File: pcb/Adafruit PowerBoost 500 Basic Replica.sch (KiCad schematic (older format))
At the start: 24 parts, among them CN1 USBA, J1 HEADER, J2 PWR OUT CONN, Q1 MMUN2133LT1G, U1 TPS61090RSAR

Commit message: Agregada la propuesta
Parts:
- BT1: footprint (none) -> Connector_JST:JST_EH_S2B-EH_1x02_P2.50mm_Horizontal
- C1, C2, C3: footprint (none) -> Capacitor_SMD:C_0805_2012Metric
- C4: footprint (none) -> Capacitor_SMD:C_1206_3216Metric
- CN1: footprint (none) -> Connector_USB:USB_A_CONNFLY_DS1095-WNR0
- D1, D2: footprint (none) -> LED_SMD:LED_0805_2012Metric
- J1: footprint (none) -> Connector_PinHeader_1.00mm:PinHeader_1x06_P1.00mm_Vertical
- J2: footprint (none) -> Connector_PinHeader_1.00mm:PinHeader_1x02_P1.00mm_Vertical
- L1: footprint (none) -> Inductor_SMD:L_TDK_VLP8040
- Q1: footprint (none) -> Package_TO_SOT_SMD:SOT-23
- R1, R10, R11, R2, R3, R4, R5, R6, R7, R8, R9: footprint (none) -> Resistor_SMD:R_0805_2012Metric
- U1: footprint (none) -> Package_DFN_QFN:QFN-16-1EP_4x4mm_P0.65mm_EP2.1x2.1mm
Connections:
- net +5V: no longer C3.1, C4.1, J2.1 (Pin_1), R4.1, U1.16 (VOUT)
- net GND: no longer U1.12 (LBO)
- net at U1.7 (PGND): now also U1.12 (LBO)
- new net: C3.1, C4.1, J2.1 (Pin_1), R4.1, U1.16 (VOUT)
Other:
- note added: "Etapa de Regulación"
- note added: "Indicador de 5V a la salida\n(encendido)"
- note added: "Indicador de Batería Baja"
- note added: "Salida Cargador USB"
- moved on the sheet: BT1, C1, C2, C3, C4, CN1, D1, D2, J1, J2, L1, Q1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

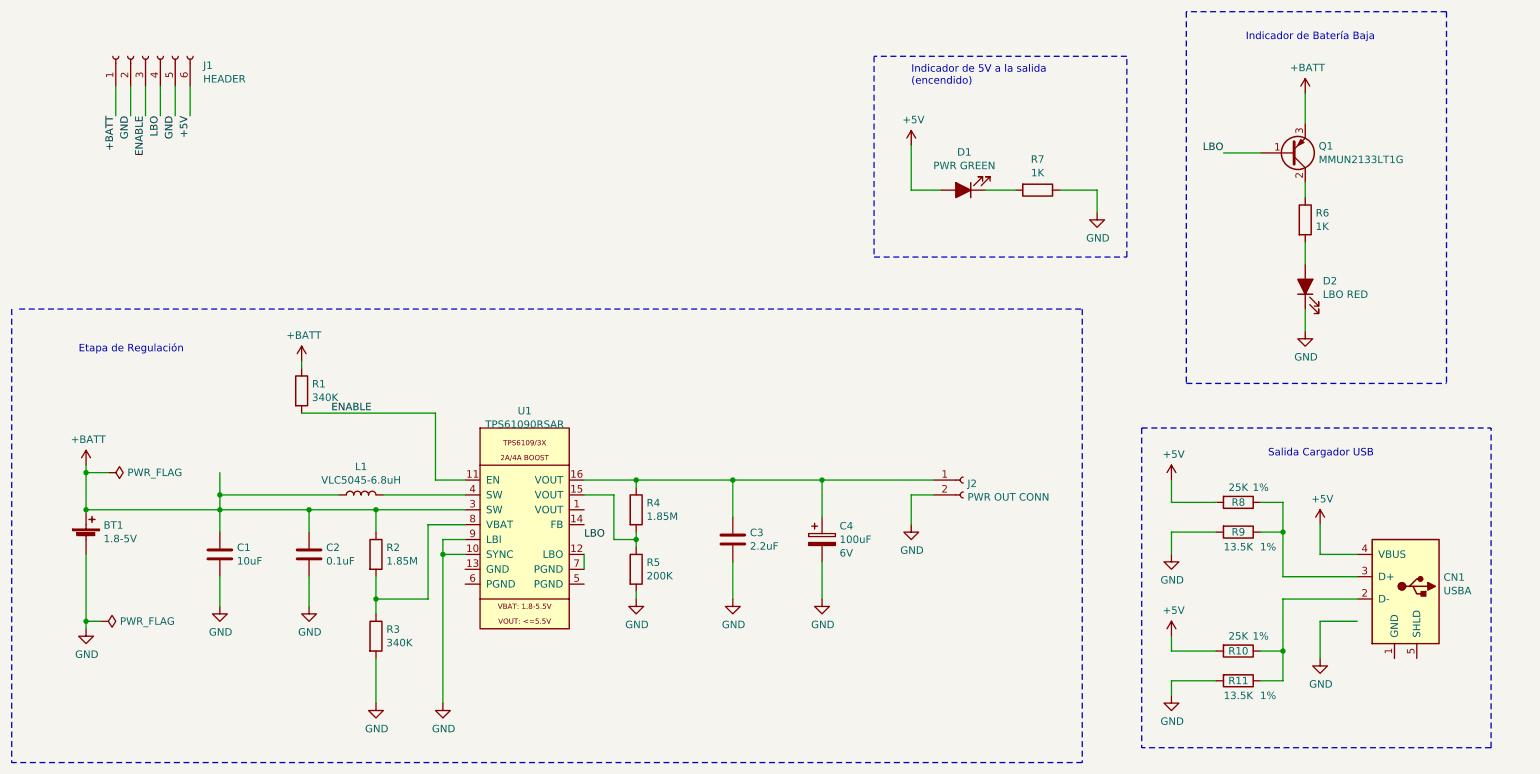
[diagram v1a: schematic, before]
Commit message: Correcciones de acuerdo a checklist esquematico
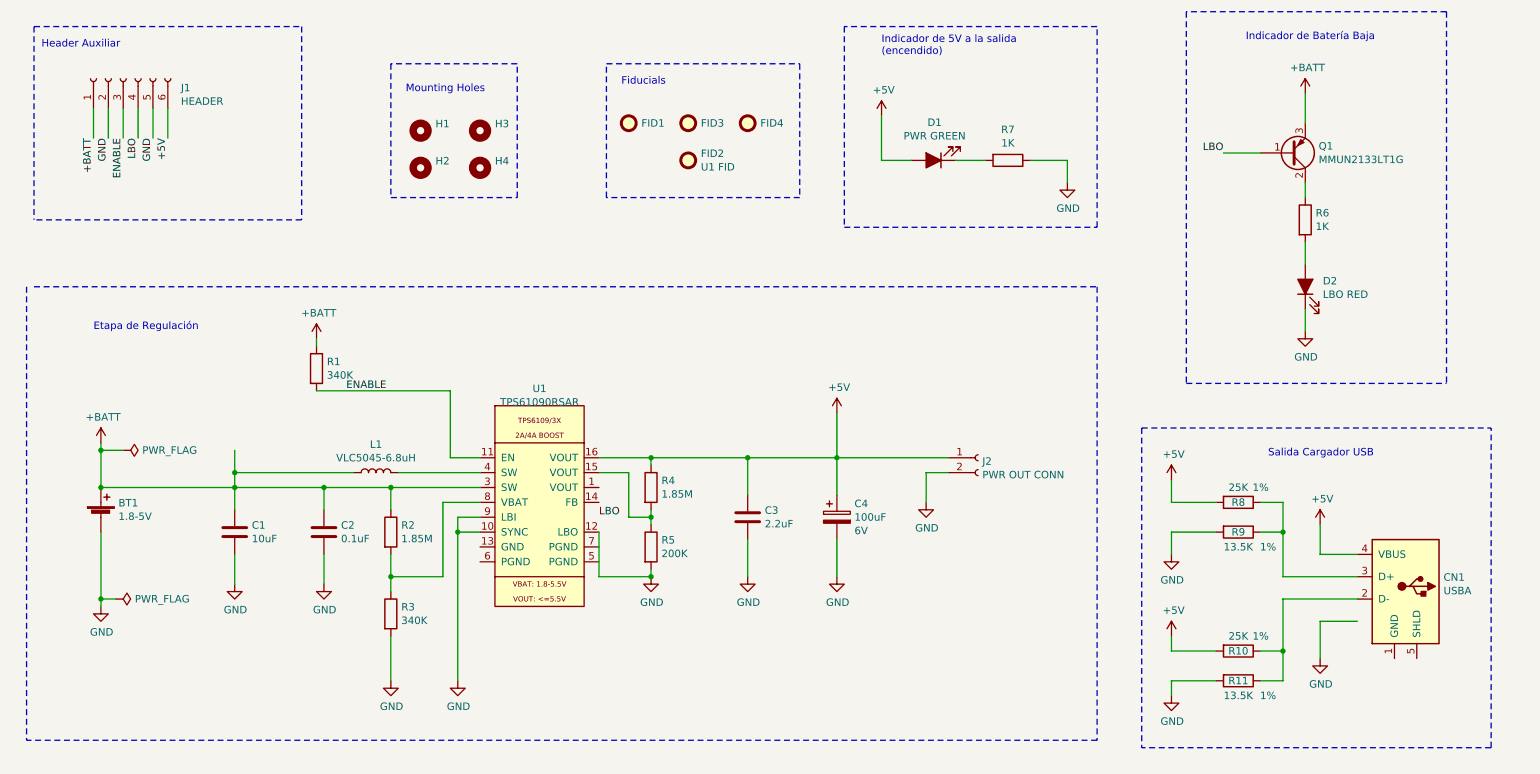
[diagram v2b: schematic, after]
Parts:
- added FID1, FID3, FID4: Fiducial, Fiducial:Fiducial_1mm_Mask2mm, symbol Mechanical:Fiducial
- added FID2: U1 FID, Fiducial:Fiducial_0.5mm_Mask1mm, symbol Mechanical:Fiducial
- added H1, H2: Mounting Hole, MountingHole:MountingHole_3mm, symbol Mechanical:MountingHole
- added H3, H4: MountingHole, MountingHole:MountingHole_3mm, symbol Mechanical:MountingHole
- J1: footprint Connector_PinHeader_1.00mm:PinHeader_1x06_P1.00mm_Vertical -> Connector_PinSocket_1.00mm:PinSocket_1x06_P1.00mm_Vertical
- Q1: Mouser N (none) -> 863-MMUN2111LT1G
- U1: Mouser Num (none) -> 595-TPS61090RSAR
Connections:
- net +5V: now also C3.1, C4.1, J2.1 (Pin_1), R4.1, U1.16 (VOUT)
- net GND: now also U1.12 (LBO)
- net at U1.7 (PGND): no longer U1.12 (LBO)
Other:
- note added: "Fiducials"
- note added: "Header Auxiliar"
- note added: "Mounting Holes"
- moved on the sheet: BT1, C1, C2, C3, C4, D1, J1, J2, L1, R1, R2, R3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

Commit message: Posicionamiento tentativo
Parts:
- removed BT1: 1.8-5V, Connector_JST:JST_EH_S2B-EH_1x02_P2.50mm_Horizontal, symbol Device:Battery_Cell
- added J3: Batería, symbol Connector_Generic:Conn_01x02
- J1: symbol Connector:Conn_01x06_Female -> Connector_Generic:Conn_01x06
- J2: value PWR OUT CONN -> PWR OUT; symbol Connector:Conn_01x02_Female -> Connector_Generic:Conn_01x02
- Q1: symbol Device:Q_PNP_BCE -> Device:Q_PNP_BEC_BRT
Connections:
- net +5V: now also U1.1 (VOUT), U1.15 (VOUT)
- net +BATT: now also Q1.2 (E), U1.8 (VBAT), J3.2 (Pin_2); no longer Q1.3 (E), U1.3 (SW)
- net GND: now also U1.13 (GND), U1.5 (PGND), U1.6 (PGND), U1.7 (PGND), J3.1 (Pin_1); no longer U1.12 (LBO), U1.9 (LBI)
- net LBO: now also U1.12 (LBO); no longer U1.2 (NC)
- net at R2.2, R3.1: now also U1.9 (LBI); no longer U1.8 (VBAT)
- net at R4.2, R5.1: now also U1.14 (FB); no longer U1.15 (VOUT)
- net at R6.1: now also Q1.3 (C); no longer Q1.2 (C)
- net at L1.2, U1.4 (SW): now also U1.3 (SW)
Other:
- note added: "1.8-5V"
- note added: "6.8uH / 2A"
- note added: "R2 = 5.5 * R2"
- note added: "R3 < 500k"
- moved on the sheet: C1, C2, C3, C4, J2, L1, R1, R2, R3, R4, R5, U1

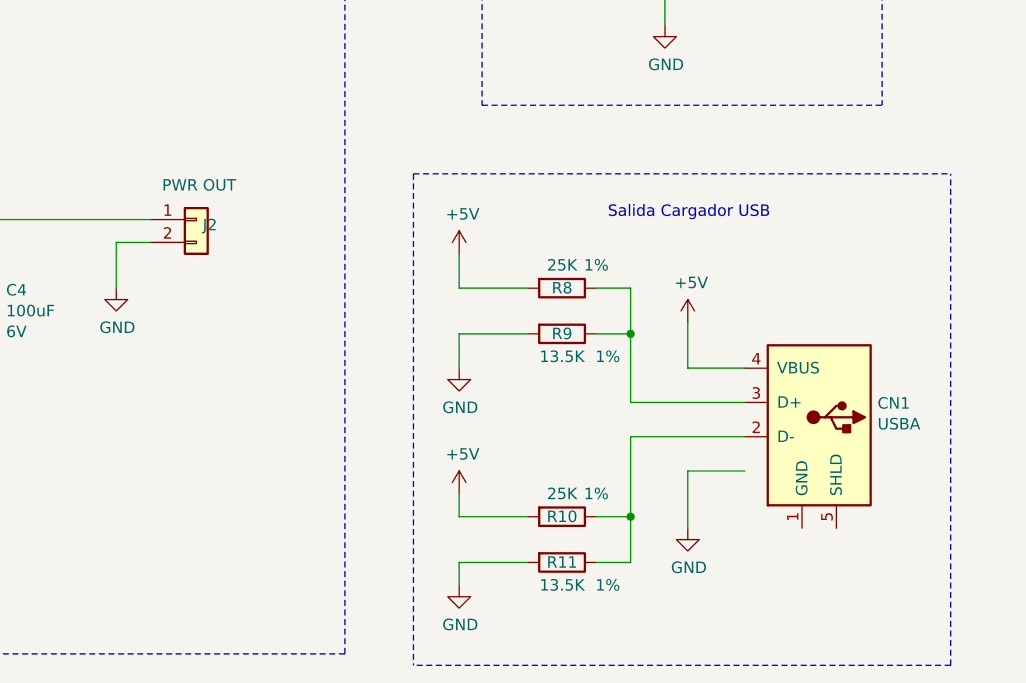
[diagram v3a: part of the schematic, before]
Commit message: Adds missing footprint 3d models
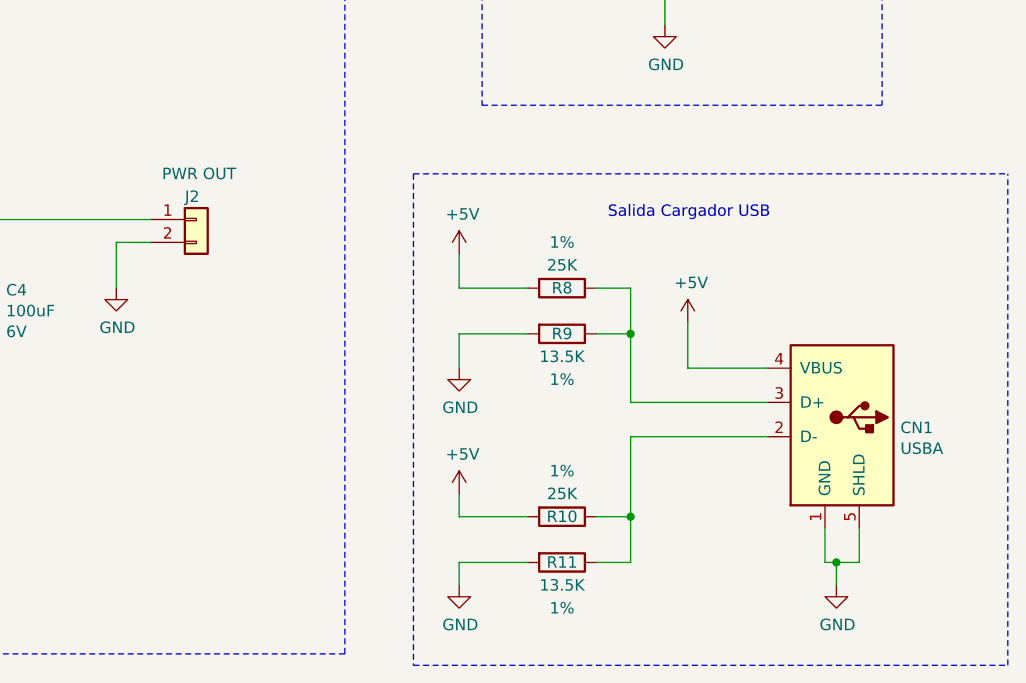
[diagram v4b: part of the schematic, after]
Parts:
- CN1: footprint Connector_USB:USB_A_CONNFLY_DS1095-WNR0 -> Connector_USB:USB_A_Molex_67643_Horizontal
- J2: footprint Connector_PinHeader_1.00mm:PinHeader_1x02_P1.00mm_Vertical -> Connector_JST:JST_EH_S2B-EH_1x02_P2.50mm_Horizontal
- J3: footprint (none) -> Connector_JST:JST_EH_S2B-EH_1x02_P2.50mm_Horizontal
- L1: footprint Inductor_SMD:L_TDK_VLP8040 -> Inductor_SMD:L_Taiyo-Yuden_MD-2020
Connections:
- net GND: now also CN1.1 (GND), CN1.5 (SHLD)
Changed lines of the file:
@@
 Wire Notes Line
 	8400 4000 8400 6150
-Wire Notes Line
-	10750 6150 8400 6150
-Wire Notes Line
-	8400 4000 10750 4000
 $Comp
 L Device:R R8
@@
 F 2 "Resistor_SMD:R_0805_2012Metric" V 8980 4500 50  0001 C CNN
 F 3 "~" H 9050 4500 50  0001 C CNN
-F 4 "1%" V 8950 4650 50  0000 C CNN "Tolerance"
+F 4 "1%" V 8850 4500 50  0000 C CNN "Tolerance"
 	1    9050 4500
 	0    1    1    0
@@
 F 2 "Resistor_SMD:R_0805_2012Metric" V 8980 4700 50  0001 C CNN
 F 3 "~" H 9050 4700 50  0001 C CNN
-F 4 "1%" V 9150 4900 50  0000 C CNN "Tolerance"
+F 4 "1%" V 9250 4700 50  0000 C CNN "Tolerance"
 	1    9050 4700
 	0    1    1    0
@@
 F 2 "Resistor_SMD:R_0805_2012Metric" V 8980 5500 50  0001 C CNN
 F 3 "~" H 9050 5500 50  0001 C CNN
-F 4 "1%" V 8950 5650 50  0000 C CNN "Tolerance"
+F 4 "1%" V 8850 5500 50  0000 C CNN "Tolerance"
 	1    9050 5500
 	0    1    1    0
@@
 F 2 "Resistor_SMD:R_0805_2012Metric" V 8980 5700 50  0001 C CNN
 F 3 "~" H 9050 5700 50  0001 C CNN
-F 4 "1%" V 9150 5900 50  0000 C CNN "Tolerance"
+F 4 "1%" V 9250 5700 50  0000 C CNN "Tolerance"
 	1    9050 5700
 	0    1    1    0
@@
 $EndComp
 $Comp
-L power:GND #PWR021
-U 1 1 613AC8FC
-P 9600 5550
-F 0 "#PWR021" H 9600 5300 50  0001 C CNN
-F 1 "GND" H 9605 5377 50  0000 C CNN
-F 2 "" H 9600 5550 50  0001 C CNN
-F 3 "" H 9600 5550 50  0001 C CNN
-	1    9600 5550
-	1    0    0    -1
-$EndComp
-$Comp
 L power:+5V #PWR020
 U 1 1 613AD33E
@@
 	8600 5700 8600 5800
 Wire Wire Line
-	9850 5000 9350 5000
-Wire Wire Line
 	9350 5000 9350 4700
 Connection ~ 9350 4700
 Wire Wire Line
 	9350 5500 9350 5150
-Wire Wire Line
-	9350 5150 9850 5150
 Connection ~ 9350 5500
 Wire Wire Line
-	9850 5300 9600 5300
-Wire Wire Line
-	9600 5300 9600 5550
-Wire Wire Line
 	9600 4650 9600 4850
-Wire Wire Line
-	9600 4850 9850 4850
 Text Notes 9250 4200 0    50   ~ 0
 Salida Cargador USB
 Wire Notes Line
-	10750 6150 10750 4000
+	11000 6150 11000 4000
 Wire Notes Line
 	10450 1200 8700 1200
@@
 F 0 "L1" V 3590 4300 50  0000 C CNN
 F 1 "VLC5045-6.8uH" V 3499 4300 50  0000 C CNN
-F 2 "Inductor_SMD:L_TDK_VLP8040" H 3400 4300 50  0001 C CNN
+F 2 "Inductor_SMD:L_Taiyo-Yuden_MD-2020" H 3400 4300 50  0001 C CNN
 F 3 "~" H 3400 4300 50  0001 C CNN
 	1    3400 4300
@@
 U 1 1 613C3CFF
 P 7450 4200
-F 0 "J2" H 7478 4176 50  0000 L CNN
-F 1 "PWR OUT" H 7300 4350 50  0000 L CNN
-F 2 "Connector_PinHeader_1.00mm:PinHeader_1x02_P1.00mm_Vertical" H 7450 4200 50  0001 C CNN
+F 0 "J2" H 7400 4300 50  0000 L CNN
+F 1 "PWR OUT" H 7300 4400 50  0000 L CNN
+F 2 "Connector_JST:JST_EH_S2B-EH_1x02_P2.50mm_Horizontal" H 7450 4200 50  0001 C CNN
 F 3 "~" H 7450 4200 50  0001 C CNN
 	1    7450 4200
@@
 F 0 "J3" H 1300 4100 50  0000 L CNN
 F 1 "Batería" H 1200 4000 50  0000 L CNN
-F 2 "" H 1350 4400 50  0001 C CNN
+F 2 "Connector_JST:JST_EH_S2B-EH_1x02_P2.50mm_Horizontal" H 1350 4400 50  0001 C CNN
 F 3 "~" H 1350 4400 50  0001 C CNN
 	1    1350 4400
@@
 Wire Notes Line style solid
 	2350 5500 3050 5500
+Wire Wire Line
+	9600 4850 9950 4850
+Wire Wire Line
+	9350 5000 9950 5000
+Wire Wire Line
+	9350 5150 9950 5150
+Wire Notes Line
+	8400 6150 11000 6150
+Wire Wire Line
+	10250 5700 10200 5700
+Wire Wire Line
+	10250 5800 10250 5700
+Wire Wire Line
+	10200 5700 10200 5550
+Connection ~ 10250 5700
+Wire Wire Line
+	10350 5700 10250 5700
+Wire Wire Line
+	10350 5550 10350 5700
+$Comp
+L power:GND #PWR021
+U 1 1 613AC8FC
+P 10250 5800
+F 0 "#PWR021" H 10250 5550 50  0001 C CNN
+F 1 "GND" H 10255 5627 50  0000 C CNN
+F 2 "" H 10250 5800 50  0001 C CNN
+F 3 "" H 10250 5800 50  0001 C CNN
+	1    10250 5800
+	1    0    0    -1
+$EndComp
 $Comp
 L AdafruitPowerBoost:USBA CN1
-U 1 1 61563A4E
-P 10100 4650
-F 0 "CN1" H 10430 4296 50  0000 L CNN
-F 1 "USBA" H 10430 4205 50  0000 L CNN
-F 2 "Connector_USB:USB_A_CONNFLY_DS1095-WNR0" H 9850 4600 50  0001 C CNN
-F 3 "" H 9850 4600 50  0001 C CNN
-	1    10100 4650
-	1    0    0    -1
-$EndComp
+U 1 1 614C579A
+P 10200 4650
+F 0 "CN1" H 10530 4189 50  0000 L CNN
+F 1 "USBA" H 10530 4098 50  0000 L CNN
+F 2 "Connector_USB:USB_A_Molex_67643_Horizontal" H 9950 4600 50  0001 C CNN
+F 3 "" H 9950 4600 50  0001 C CNN
+	1    10200 4650
+	1    0    0    -1
+$EndComp
+Wire Notes Line
+	8400 4000 11000 4000
 $EndSCHEMATC

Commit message: Agrega Ruteo
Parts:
- C1, C2, C3: footprint Capacitor_SMD:C_0805_2012Metric -> Capacitor_SMD:C_0805_2012Metric_Pad1.18x1.45mm_HandSolder
- C4: footprint Capacitor_SMD:C_1206_3216Metric -> Capacitor_SMD:C_1210_3225Metric_Pad1.33x2.70mm_HandSolder
- D1, D2: footprint LED_SMD:LED_0805_2012Metric -> LED_SMD:LED_0805_2012Metric_Pad1.15x1.40mm_HandSolder
- L1: footprint Inductor_SMD:L_Taiyo-Yuden_MD-2020 -> Inductor_SMD:L_Taiyo-Yuden_NR-40xx_HandSoldering
- R1, R10, R11, R2, R3, R4, R5, R6, R7, R8, R9: footprint Resistor_SMD:R_0805_2012Metric -> Resistor_SMD:R_0805_2012Metric_Pad1.20x1.40mm_HandSolder
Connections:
- net +5V: now also J1.5 (Pin_5); no longer J1.6 (Pin_6)
- net ENABLE: now also J1.4 (Pin_4); no longer J1.3 (Pin_3)
- net GND: now also J1.6 (Pin_6); no longer J1.5 (Pin_5)
- net LBO: now also J1.3 (Pin_3); no longer J1.4 (Pin_4)
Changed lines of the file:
@@
 Text Label 1350 2050 3    50   ~ 0
 +BATT
+Text Label 1650 2050 3    50   ~ 0
+ENABLE
 Text Label 1550 2050 3    50   ~ 0
-ENABLE
-Text Label 1650 2050 3    50   ~ 0
 LBO
+Text Label 1850 2050 3    50   ~ 0
+GND
 Text Label 1750 2050 3    50   ~ 0
-GND
-Text Label 1850 2050 3    50   ~ 0
 +5V
 Text Label 1450 2050 3    50   ~ 0
@@
 F 0 "D1" H 6993 1945 50  0000 C CNN
 F 1 "PWR GREEN" H 6993 2036 50  0000 C CNN
-F 2 "LED_SMD:LED_0805_2012Metric" H 7000 2200 50  0001 C CNN
+F 2 "LED_SMD:LED_0805_2012Metric_Pad1.15x1.40mm_HandSolder" H 7000 2200 50  0001 C CNN
 F 3 "~" H 7000 2200 50  0001 C CNN
 	1    7000 2200
@@
 F 0 "R7" V 7293 2200 50  0000 C CNN
 F 1 "1K" V 7384 2200 50  0000 C CNN
-F 2 "Resistor_SMD:R_0805_2012Metric" V 7430 2200 50  0001 C CNN
+F 2 "Resistor_SMD:R_0805_2012Metric_Pad1.20x1.40mm_HandSolder" V 7430 2200 50  0001 C CNN
 F 3 "~" H 7500 2200 50  0001 C CNN
 	1    7500 2200
@@
 F 0 "R8" V 9050 4500 50  0000 C CNN
 F 1 "25K" V 8950 4500 50  0000 C CNN
-F 2 "Resistor_SMD:R_0805_2012Metric" V 8980 4500 50  0001 C CNN
+F 2 "Resistor_SMD:R_0805_2012Metric_Pad1.20x1.40mm_HandSolder" V 8980 4500 50  0001 C CNN
 F 3 "~" H 9050 4500 50  0001 C CNN
 F 4 "1%" V 8850 4500 50  0000 C CNN "Tolerance"
@@
 F 0 "R9" V 9050 4700 50  0000 C CNN
 F 1 "13.5K" V 9150 4700 50  0000 C CNN
-F 2 "Resistor_SMD:R_0805_2012Metric" V 8980 4700 50  0001 C CNN
+F 2 "Resistor_SMD:R_0805_2012Metric_Pad1.20x1.40mm_HandSolder" V 8980 4700 50  0001 C CNN
 F 3 "~" H 9050 4700 50  0001 C CNN
 F 4 "1%" V 9250 4700 50  0000 C CNN "Tolerance"
@@
 F 0 "R10" V 9050 5500 50  0000 C CNN
 F 1 "25K" V 8950 5500 50  0000 C CNN
-F 2 "Resistor_SMD:R_0805_2012Metric" V 8980 5500 50  0001 C CNN
+F 2 "Resistor_SMD:R_0805_2012Metric_Pad1.20x1.40mm_HandSolder" V 8980 5500 50  0001 C CNN
 F 3 "~" H 9050 5500 50  0001 C CNN
 F 4 "1%" V 8850 5500 50  0000 C CNN "Tolerance"
@@
 F 0 "R11" V 9050 5700 50  0000 C CNN
 F 1 "13.5K" V 9150 5700 50  0000 C CNN
-F 2 "Resistor_SMD:R_0805_2012Metric" V 8980 5700 50  0001 C CNN
+F 2 "Resistor_SMD:R_0805_2012Metric_Pad1.20x1.40mm_HandSolder" V 8980 5700 50  0001 C CNN
 F 3 "~" H 9050 5700 50  0001 C CNN
 F 4 "1%" V 9250 5700 50  0000 C CNN "Tolerance"
@@
 F 0 "R6" H 9570 2646 50  0000 L CNN
 F 1 "1K" H 9570 2555 50  0000 L CNN
-F 2 "Resistor_SMD:R_0805_2012Metric" V 9430 2600 50  0001 C CNN
+F 2 "Resistor_SMD:R_0805_2012Metric_Pad1.20x1.40mm_HandSolder" V 9430 2600 50  0001 C CNN
 F 3 "~" H 9500 2600 50  0001 C CNN
 	1    9500 2600
@@
 F 0 "D2" V 9539 2932 50  0000 R CNN
 F 1 "LBO RED" V 9448 2932 50  0000 R CNN
-F 2 "LED_SMD:LED_0805_2012Metric" H 9500 3050 50  0001 C CNN
+F 2 "LED_SMD:LED_0805_2012Metric_Pad1.15x1.40mm_HandSolder" H 9500 3050 50  0001 C CNN
 F 3 "~" H 9500 3050 50  0001 C CNN
 	1    9500 3050
@@
 F 0 "R5" H 5320 4846 50  0000 L CNN
 F 1 "200K" H 5320 4755 50  0000 L CNN
-F 2 "Resistor_SMD:R_0805_2012Metric" V 5180 4800 50  0001 C CNN
+F 2 "Resistor_SMD:R_0805_2012Metric_Pad1.20x1.40mm_HandSolder" V 5180 4800 50  0001 C CNN
 F 3 "~" H 5250 4800 50  0001 C CNN
 	1    5250 4800
@@
 F 0 "C3" H 6015 4646 50  0000 L CNN
 F 1 "2.2uF" H 6015 4555 50  0000 L CNN
-F 2 "Capacitor_SMD:C_0805_2012Metric" H 5938 4450 50  0001 C CNN
+F 2 "Capacitor_SMD:C_0805_2012Metric_Pad1.18x1.45mm_HandSolder" H 5938 4450 50  0001 C CNN
 F 3 "~" H 5900 4600 50  0001 C CNN
 	1    5900 4600
@@
 F 0 "C4" H 6618 4691 50  0000 L CNN
 F 1 "100uF" H 6618 4600 50  0000 L CNN
-F 2 "Capacitor_SMD:C_1206_3216Metric" H 6538 4450 50  0001 C CNN
+F 2 "Capacitor_SMD:C_1210_3225Metric_Pad1.33x2.70mm_HandSolder" H 6538 4450 50  0001 C CNN
 F 3 "~" H 6500 4600 50  0001 C CNN
 F 4 "6V" H 6618 4509 50  0000 L CNN "Voltage"
@@
 F 0 "C1" H 2565 4746 50  0000 L CNN
 F 1 "10uF" H 2565 4655 50  0000 L CNN
-F 2 "Capacitor_SMD:C_0805_2012Metric" H 2488 4550 50  0001 C CNN
+F 2 "Capacitor_SMD:C_0805_2012Metric_Pad1.18x1.45mm_HandSolder" H 2488 4550 50  0001 C CNN
 F 3 "~" H 2450 4700 50  0001 C CNN
 	1    2450 4700
@@
 F 0 "L1" V 3590 4300 50  0000 C CNN
 F 1 "VLC5045-6.8uH" V 3499 4300 50  0000 C CNN
-F 2 "Inductor_SMD:L_Taiyo-Yuden_MD-2020" H 3400 4300 50  0001 C CNN
+F 2 "Inductor_SMD:L_Taiyo-Yuden_NR-40xx_HandSoldering" H 3400 4300 50  0001 C CNN
 F 3 "~" H 3400 4300 50  0001 C CNN
 	1    3400 4300
@@
 F 0 "C2" H 3165 4746 50  0000 L CNN
 F 1 "0.1uF" H 3165 4655 50  0000 L CNN
-F 2 "Capacitor_SMD:C_0805_2012Metric" H 3088 4550 50  0001 C CNN
+F 2 "Capacitor_SMD:C_0805_2012Metric_Pad1.18x1.45mm_HandSolder" H 3088 4550 50  0001 C CNN
 F 3 "~" H 3050 4700 50  0001 C CNN
 	1    3050 4700
@@
 F 0 "R4" H 5320 4446 50  0000 L CNN
 F 1 "1.85M" H 5320 4355 50  0000 L CNN
-F 2 "Resistor_SMD:R_0805_2012Metric" V 5180 4400 50  0001 C CNN
+F 2 "Resistor_SMD:R_0805_2012Metric_Pad1.20x1.40mm_HandSolder" V 5180 4400 50  0001 C CNN
 F 3 "~" H 5250 4400 50  0001 C CNN
 	1    5250 4400
@@
 F 0 "R1" H 3070 3646 50  0000 L CNN
 F 1 "340K" H 3070 3555 50  0000 L CNN
-F 2 "Resistor_SMD:R_0805_2012Metric" V 2930 3600 50  0001 C CNN
+F 2 "Resistor_SMD:R_0805_2012Metric_Pad1.20x1.40mm_HandSolder" V 2930 3600 50  0001 C CNN
 F 3 "~" H 3000 3600 50  0001 C CNN
 	1    3000 3600
@@
 F 0 "R3" H 3570 5196 50  0000 L CNN
 F 1 "340K" H 3570 5105 50  0000 L CNN
-F 2 "Resistor_SMD:R_0805_2012Metric" V 3430 5150 50  0001 C CNN
+F 2 "Resistor_SMD:R_0805_2012Metric_Pad1.20x1.40mm_HandSolder" V 3430 5150 50  0001 C CNN
 F 3 "~" H 3500 5150 50  0001 C CNN
 	1    3500 5150
@@
 F 0 "R2" H 3570 4746 50  0000 L CNN
 F 1 "1.85M" H 3570 4655 50  0000 L CNN
-F 2 "Resistor_SMD:R_0805_2012Metric" V 3430 4700 50  0001 C CNN
+F 2 "Resistor_SMD:R_0805_2012Metric_Pad1.20x1.40mm_HandSolder" V 3430 4700 50  0001 C CNN
 F 3 "~" H 3500 4700 50  0001 C CNN
 	1    3500 4700
